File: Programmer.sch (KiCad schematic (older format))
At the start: 59 parts, among them CON1 USB_OTG, M1 ESP-12E, P1 Test, P3 CONN_12, Q1 MMBT3904, Q2 MMBT3906, Q3 MMBT3904, SW1 Upload, SW2 RESET, U1 AP2112K-3.3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

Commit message: Desing Review V00B
Corrections made from doing a Design Review.
Now at revision 00B
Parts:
- removed P1: Test, Measurement_Points:Measurement_Point_Square-TH_Big, symbol CONN_01X01
- added C17: 100 µF, Capacitors_SMD:C_1206_HandSoldering, symbol C
- added C20: 0.1 µF, Capacitors_SMD:C_1206_HandSoldering, symbol C
- added P1: CONN_01X12, symbol CONN_01X12
- added R10, R17, R18, R7: 1K, symbol R
- added R5: 10, symbol R
- C15: value 0.1. µF -> 0.1 µF
- gave numbers to parts that had none: 11
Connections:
- net labels added: IO2, IO3, MISO, MOSI, Pulse, SCK
- wire segments 312 -> 345
- no-connect marks 10 -> 6
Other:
- moved on the sheet: C11, C14, D1, L1, Q4, Q5, R6, R8, R9

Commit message: Re-layout Update V00B
Multiple changes to the schematic and PCB component placement, complete
re-route of PCB.
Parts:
- removed C15, C8, C9: 0.1 µF, Capacitors_SMD:C_1206_HandSoldering, symbol C
- removed U3, U4, U5, U6: 74LVC2T45, Housings_SSOP:MSOP-8_3x3mm_Pitch0.65mm, symbol 74LVC2T45
- removed U7: 74HC595, SMD_Packages:SO-16-N, symbol 74HC595
- added U3: FXMA108, Uprogrammer FPs:DQFN20, symbol FXMA108
- C1, C10, C11, C12, C13, C14, C16, C17, C18, C19, C2, C20, C3, C4, C5, C6, C7: footprint Capacitors_SMD:C_1206_HandSoldering -> Capacitors_SMD:C_1206
- L1: footprint Choke_SMD:Choke_SMD_1206_Handsoldering -> Choke_SMD:Choke_SMD_1206_Standard
- P1: footprint (none) -> Socket_Strips:Socket_Strip_Straight_1x12
- Q4, Q5: footprint (none) -> Housings_SOT-23_SOT-143_TSOT-6:SOT-23
- R1, R11, R12, R13, R14, R15, R16, R19, R2, R20, R3, R4, R6, R8, R9: footprint Resistors_SMD:R_1206_HandSoldering -> Resistors_SMD:R_1206
- R10, R17, R18, R5, R7: footprint (none) -> Resistors_SMD:R_1206
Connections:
- net labels added: Vpf
- net labels removed: D0, D1, D2, D3
- wire segments 345 -> 227
- no-connect marks 6 -> 4
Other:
- note removed: "Assign Pin 11 to VPP \nonce Implimented"
- moved on the sheet: C6

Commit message: V00b PCB fixes
Fixes needed to repair mistakes in PCB design.
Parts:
- removed Q1, Q6, Q7: MMBT3904, Housings_SOT-23_SOT-143_TSOT-6:SOT-23, symbol MMBT3904
- added Q1: BSS138L, Housings_SOT-23_SOT-143_TSOT-6:SOT-23, symbol Q_NMOS_GSD
- R8: value 58.2K -> 100K
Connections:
- wire segments 227 -> 219
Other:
- moved on the sheet: C12, C13, C3, R20
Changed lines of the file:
@@
 P 4875 6525
 F 0 "R8" H 4975 6575 50  0000 C CNN
-F 1 "58.2K" H 5025 6475 50  0000 C CNN
+F 1 "100K" H 5025 6475 50  0000 C CNN
 F 2 "Resistors_SMD:R_1206" V 4805 6525 30  0001 C CNN
 F 3 "" H 4875 6525 30  0000 C CNN
@@
 	2550 2200 2450 2200
 Wire Wire Line
-	2450 2200 2450 2050
+	2450 2050 2450 2200
 Connection ~ 2450 2050
 Connection ~ 2300 2050
@@
 Wire Wire Line
 	6400 700  7550 700
-$Comp
-L MMBT3904 Q1
-U 1 1 55D843D6
-P 8700 4600
-F 0 "Q1" H 8900 4675 50  0000 L CNN
-F 1 "MMBT3904" H 8900 4600 50  0000 L CNN
-F 2 "Housings_SOT-23_SOT-143_TSOT-6:SOT-23" H 8900 4525 50  0001 L CIN
-F 3 "" H 8700 4600 50  0000 L CNN
-	1    8700 4600
-	1    0    0    -1
-$EndComp
 $Comp
 L MMBT3904 Q3
@@
 	4375 3000 4375 2600
 Connection ~ 4375 2600
-Wire Wire Line
-	5600 4300 5950 4300
 Connection ~ 5950 1400
 Wire Wire Line
@@
 ~RST
 $Comp
-L MMBT3904 Q6
-U 1 1 563E70E3
-P 5150 4200
-F 0 "Q6" H 5350 4275 50  0000 L CNN
-F 1 "MMBT3904" H 5350 4200 50  0000 L CNN
-F 2 "Housings_SOT-23_SOT-143_TSOT-6:SOT-23" H 5350 4125 50  0001 L CIN
-F 3 "" H 5150 4200 50  0000 L CNN
-	1    5150 4200
-	1    0    0    -1
-$EndComp
-$Comp
 L R R19
 U 1 1 563E70E9
@@
 $EndComp
 Wire Wire Line
-	4850 4200 4950 4200
-$Comp
-L MMBT3904 Q7
-U 1 1 563E7206
-P 5500 4600
-F 0 "Q7" H 5750 4725 50  0000 L CNN
-F 1 "MMBT3904" H 5725 4650 50  0000 L CNN
-F 2 "Housings_SOT-23_SOT-143_TSOT-6:SOT-23" H 5700 4525 50  0001 L CIN
-F 3 "" H 5500 4600 50  0000 L CNN
-	1    5500 4600
-	1    0    0    -1
-$EndComp
+	4850 4200 5125 4200
 $Comp
 L R R20
 U 1 1 563E720C
-P 5050 4600
-F 0 "R20" V 4900 4575 50  0000 C CNN
-F 1 "10K" V 4975 4575 50  0000 C CNN
-F 2 "Resistors_SMD:R_1206" V 4980 4600 30  0001 C CNN
-F 3 "" H 5050 4600 30  0000 C CNN
-	1    5050 4600
-	0    1    1    0
-$EndComp
-Wire Wire Line
-	5200 4600 5300 4600
-$Comp
-L GND #PWR022
-U 1 1 563E73B6
-P 5600 4850
-F 0 "#PWR022" H 5600 4850 30  0001 C CNN
-F 1 "GND" H 5600 4780 30  0001 C CNN
-F 2 "" H 5600 4850 60  0000 C CNN
-F 3 "" H 5600 4850 60  0000 C CNN
-	1    5600 4850
-	1    0    0    -1
-$EndComp
-$Comp
-L GND #PWR023
-U 1 1 563E7504
-P 5250 4450
-F 0 "#PWR023" H 5250 4450 30  0001 C CNN
-F 1 "GND" H 5250 4380 30  0001 C CNN
-F 2 "" H 5250 4450 60  0000 C CNN
-F 3 "" H 5250 4450 60  0000 C CNN
-	1    5250 4450
-	1    0    0    -1
-$EndComp
-Wire Wire Line
-	5250 4400 5250 4450
-Wire Wire Line
-	5600 4800 5600 4850
-Wire Wire Line
-	4400 4300 4800 4300
+P 5350 4300
+F 0 "R20" V 5200 4275 50  0000 C CNN
+F 1 "10K" V 5275 4275 50  0000 C CNN
+F 2 "Resistors_SMD:R_1206" V 5280 4300 30  0001 C CNN
+F 3 "" H 5350 4300 30  0000 C CNN
+	1    5350 4300
+	0    1    1    0
+$EndComp
 Wire Wire Line
 	4400 4200 4550 4200
-Wire Wire Line
-	5250 3950 5425 3950
-Text Label 5275 3950 0    60   ~ 0
+Text Label 4975 4200 0    60   ~ 0
 ~RST
-$Comp
-L +BATT #PWR024
-U 1 1 563ED62D
-P 4500 3850
-F 0 "#PWR024" H 4500 3800 20  0001 C CNN
-F 1 "+BATT" H 4500 3950 30  0000 C CNN
-F 2 "" H 4500 3850 60  0000 C CNN
-F 3 "" H 4500 3850 60  0000 C CNN
-	1    4500 3850
-	1    0    0    -1
-$EndComp
 Wire Wire Line
 	4500 4000 4400 4000
@@
 Connection ~ 2775 6275
 Connection ~ 3175 6600
-Wire Wire Line
-	5600 4300 5600 4400
-Wire Wire Line
-	4800 4300 4800 4600
-Wire Wire Line
-	4800 4600 4900 4600
-Wire Wire Line
-	5250 3950 5250 4000
 $Comp
 L C C3
 U 1 1 563DA479
-P 3375 4000
-F 0 "C3" V 3225 3850 40  0000 L CNN
-F 1 "0.1 µF" V 3275 3850 40  0000 L CNN
-F 2 "Capacitors_SMD:C_1206" H 3413 3850 30  0001 C CNN
-F 3 "~" H 3375 4000 60  0000 C CNN
-	1    3375 4000
-	0    1    1    0
-$EndComp
-Wire Wire Line
-	3225 4000 2975 4000
+P 3250 4000
+F 0 "C3" V 3100 3850 40  0000 L CNN
+F 1 "0.1 µF" V 3150 3850 40  0000 L CNN
+F 2 "Capacitors_SMD:C_1206" H 3288 3850 30  0001 C CNN
+F 3 "~" H 3250 4000 60  0000 C CNN
+	1    3250 4000
+	0    1    1    0
+$EndComp
+Wire Wire Line
+	3100 4000 2975 4000
 Connection ~ 2975 4600
 Wire Wire Line
-	3525 4000 3600 4000
+	3400 4000 3600 4000
 $Comp
 L C C12
 U 1 1 563E29A5
-P 3375 3475
-F 0 "C12" V 3225 3325 40  0000 L CNN
-F 1 "10 µF" V 3275 3325 40  0000 L CNN
-F 2 "Capacitors_SMD:C_1206" H 3413 3325 30  0001 C CNN
-F 3 "~" H 3375 3475 60  0000 C CNN
-	1    3375 3475
+P 3250 3475
+F 0 "C12" V 3100 3325 40  0000 L CNN
+F 1 "10 µF" V 3150 3325 40  0000 L CNN
+F 2 "Capacitors_SMD:C_1206" H 3288 3325 30  0001 C CNN
+F 3 "~" H 3250 3475 60  0000 C CNN
+	1    3250 3475
 	0    1    1    0
 $EndComp
@@
 L C C13
 U 1 1 563E2B59
-P 3375 3725
-F 0 "C13" V 3225 3575 40  0000 L CNN
-F 1 "0.1 µF" V 3275 3575 40  0000 L CNN
-F 2 "Capacitors_SMD:C_1206" H 3413 3575 30  0001 C CNN
-F 3 "~" H 3375 3725 60  0000 C CNN
-	1    3375 3725
-	0    1    1    0
-$EndComp
-Wire Wire Line
-	3225 3475 2975 3475
+P 3250 3725
+F 0 "C13" V 3100 3575 40  0000 L CNN
+F 1 "0.1 µF" V 3150 3575 40  0000 L CNN
+F 2 "Capacitors_SMD:C_1206" H 3288 3575 30  0001 C CNN
+F 3 "~" H 3250 3725 60  0000 C CNN
+	1    3250 3725
+	0    1    1    0
+$EndComp
+Wire Wire Line
+	3100 3475 2975 3475
 Connection ~ 2975 4000
 Wire Wire Line
-	3225 3725 2975 3725
+	3100 3725 2975 3725
 Connection ~ 2975 3725
 Wire Wire Line
-	3525 3725 4025 3725
+	3400 3725 4025 3725
 Wire Wire Line
 	4025 3725 4025 3900
@@
 Connection ~ 4500 3900
 Wire Wire Line
-	3525 3475 3575 3475
-Wire Wire Line
-	3575 3475 3575 3725
-Connection ~ 3575 3725
+	3400 3475 3525 3475
+Wire Wire Line
+	3525 3475 3525 4000
+Connection ~ 3525 3725
 NoConn ~ 3600 4100
 Wire Wire Line
@@
 	6800 1900 6800 3400
 Wire Wire Line
-	6900 2300 5900 2300
+	5900 2300 6900 2300
 Wire Wire Line
 	6700 3300 6700 2300
@@
 Wire Wire Line
 	6100 4600 8100 4600
+$Comp
+L Q_NMOS_GSD Q1
+U 1 1 5688527A
+P 8700 4600
+F 0 "Q1" H 8550 4825 50  0000 R CNN
+F 1 "BSS138L" H 8775 4750 50  0000 R CNN
+F 2 "Housings_SOT-23_SOT-143_TSOT-6:SOT-23" H 8900 4700 29  0001 C CNN
+F 3 "" H 8700 4600 60  0000 C CNN
+	1    8700 4600
+	1    0    0    -1
+$EndComp
+Wire Wire Line
+	5950 4300 5500 4300
+Wire Wire Line
+	5200 4300 4400 4300
+Connection ~ 3525 4000
+$Comp
+L 3V3 #PWR?
+U 1 1 56893110
+P 4500 3850
+F 0 "#PWR?" H 4500 3950 40  0001 C CNN
+F 1 "3V3" H 4500 3975 40  0000 C CNN
+F 2 "" H 4500 3850 60  0000 C CNN
+F 3 "" H 4500 3850 60  0000 C CNN
+	1    4500 3850
+	1    0    0    -1
+$EndComp
 $EndSCHEMATC

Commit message: Hardware V00C
Design Update to start testing a lithium polimer cell as my power
source. Added a charge management IC that charges as well as supplies
system voltage.
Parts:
- removed BT1: BATTERY, Connect:PINHEAD1-2, symbol BATTERY
- added BT1: LiPo, symbol Single_cell
- added C15, C8: 1 µF, Capacitors_SMD:C_1206, symbol C
- added C9: 0.1 uF, Capacitors_SMD:C_1206, symbol C
- added D2: Red, symbol Led_Small
- added D3: Green, symbol Led_Small
- added D4: SD103, Diodes_SMD:SOD-323, symbol D_Schottky_Small
- added Q6: MMBT3906, Housings_SOT-23_SOT-143_TSOT-6:SOT-23, symbol MMBT3906
- added R21: 150K, symbol R
- added R22, R26: 100K, symbol R
- added R23: 10K, symbol R
- added R24, R25: 200, symbol R
- added R27: 22K, symbol R
- added U4: AAT3672-4.2-1, symbol AAT3672-4.2-1
- R4: value 10K -> 22K
- R5: value 10 -> 1K
- U8: symbol CH340G -> CH340G-RESCUE-Programmer
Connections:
- net labels added: +5V, MTDO
- wire segments 219 -> 265
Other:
- moved on the sheet: C1, C10, C11, C12, C13, C14, C16, C17, C18, C19, C2, C20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

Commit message: Hardware V00D
Revisions found during design review
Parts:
- removed R19, R20: 10K, Resistors_SMD:R_1206, symbol R
- added L2: 2.2 µH, Choke_SMD:Choke_SMD_1206_Standard, symbol INDUCTOR
- added Q? (x2): MMBT3904, Housings_SOT-23_SOT-143_TSOT-6:SOT-23, symbol MMBT3904
- added R? (x2): 10K, Resistors_SMD:R_1206, symbol R
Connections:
- net GND: now also L2.2; no longer C11.2, C14.2, C17.2, C20.2, Q5.2 (S), R9.2
- net at U8.13 (~DTR): now also Q?.2 (E), R?.2
- net at U8.14 (~RTS): now also Q?.2 (E), R?.2
- new net: Q?.1 (B), R?.1 (x2)
- new net GNDpp: C11.2, C14.2, C17.2, C20.2, L2.1, Q5.2 (S), R9.2
- no-connect marks 4 -> 2
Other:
- note added: "If U2 doesn't seem to work \nor is unreliable R27 may \nbe too big"
- note added: "The level shifter needs tested."
- moved on the sheet: C11, C14, C17, C20, D1, L1, Q4, Q5, R5, R6, R8, R9

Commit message: New Layout V00E
Updated layout with newest schematic design.
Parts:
- removed R1: 10K, Resistors_SMD:R_1206, symbol R
- removed SW1: Upload, Buttons_Switches_SMD:SW_SPST_PTS645, symbol SW_PUSH
- added C21: 10 µF, Capacitors_SMD:C_1206, symbol C
- BT1: footprint (none) -> Connect:PINHEAD1-2
- D2, D3: footprint (none) -> LEDs:LED_1206
- Q1, Q2, Q3, Q4, Q5, Q6: footprint Housings_SOT-23_SOT-143_TSOT-6:SOT-23 -> TO_SOT_Packages_SMD:SOT-23
- Q7, Q8: renamed from Q?; footprint Housings_SOT-23_SOT-143_TSOT-6:SOT-23 -> TO_SOT_Packages_SMD:SOT-23
- R21, R22, R23, R24, R25, R26, R27: footprint (none) -> Resistors_SMD:R_1206
- U1: footprint Housings_SOT-23_SOT-143_TSOT-6:SOT-23-5 -> TO_SOT_Packages_SMD:SOT-23-5
- U10: footprint Housings_SOT-23_SOT-143_TSOT-6:SC-70-6_Handsoldering -> TO_SOT_Packages_SMD:SC-70-6
- U4: footprint (none) -> UprogrammerFPs:DFN-14-1EP_3x3mm_Pitch0.4mm
- gave numbers to parts that had none: 2
- renumbered SW2 to SW1
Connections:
- net +5V: no longer U4.8 (ENBAT)
- net GND: now also C21.2
- net ~RST: now also Q7.3 (C)
- net at M1.18 (GPIO0), U10.6: now also Q8.3 (C)
- net at BT1.1, U4.12 (BAT): now also U4.8 (ENBAT), C21.1
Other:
- moved on the sheet: BT1, R23

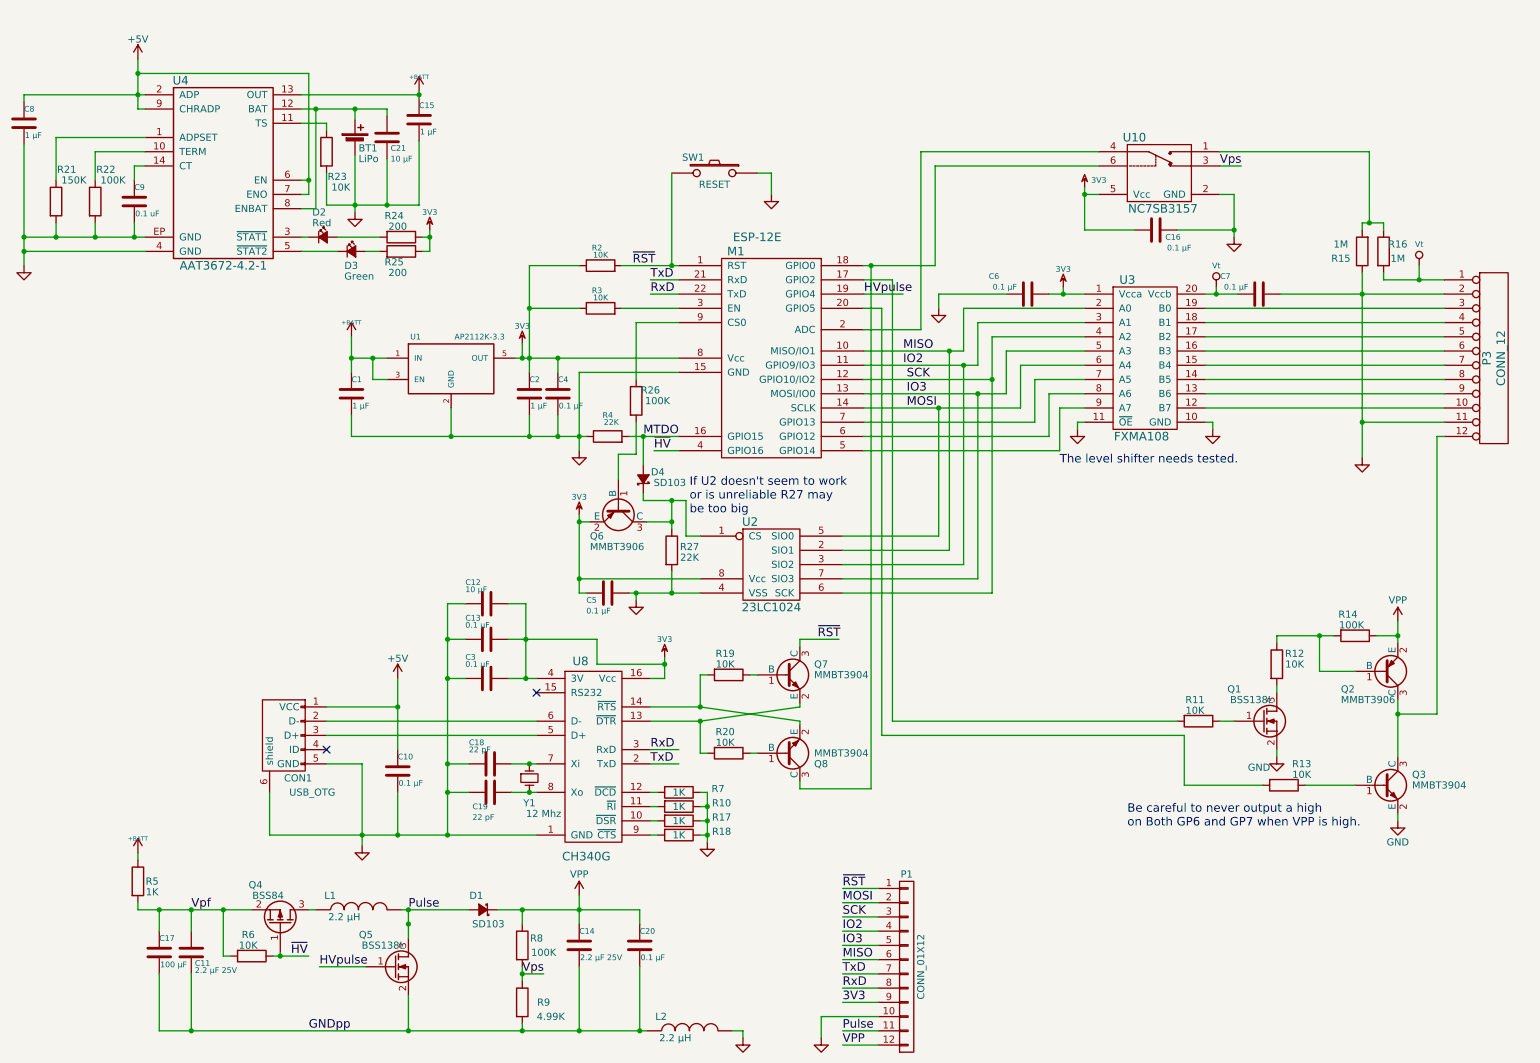
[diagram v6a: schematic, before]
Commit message: Hardware V00G
Changed value of R5 from 100 to 47 Ohms. This improves the voltage boost
functionality.
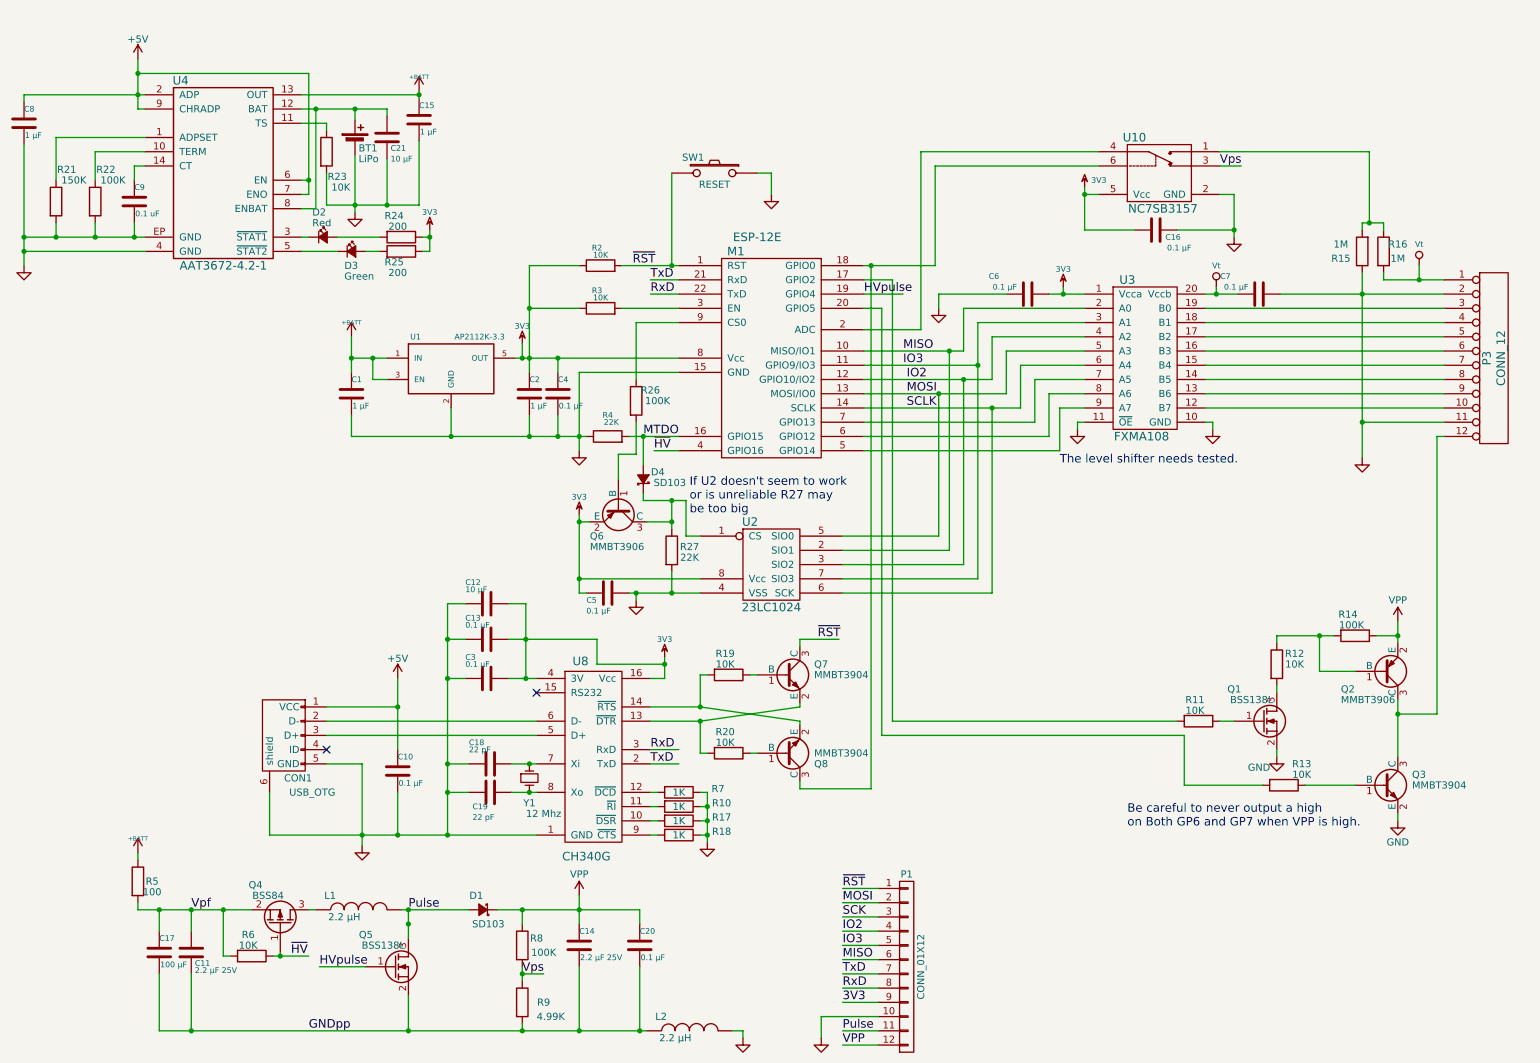
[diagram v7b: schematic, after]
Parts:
- R5: value 1K -> 100
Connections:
- net IO2: now also M1.12 (GPIO10/IO2), U3.4 (A2); no longer M1.11 (GPIO9/IO3), U3.3 (A1)
- net IO3: now also M1.11 (GPIO9/IO3), U3.3 (A1); no longer M1.13 (MOSI/IO0), U3.5 (A3)
- net MOSI: now also M1.13 (MOSI/IO0), U3.5 (A3); no longer M1.14 (SCLK), U3.6 (A4)
- net SCK: no longer M1.12 (GPIO10/IO2), U2.6 (SCK), U3.4 (A2)
- new net SCLK: M1.14 (SCLK), U2.6 (SCK), U3.6 (A4)
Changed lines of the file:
@@
 SCK
 Text Label 6800 3025 0    60   ~ 0
-SCK
+IO2
 Text Label 6800 3225 0    60   ~ 0
-MOSI
+SCLK
 Text Label 6775 2825 0    60   ~ 0
 MISO
 Text Label 6775 2925 0    60   ~ 0
-IO2
+IO3
 Text Label 6800 3125 0    60   ~ 0
-IO3
+MOSI
 Text Label 6350 6700 0    60   ~ 0
 MOSI
@@
 P 1400 6550
 F 0 "R5" H 1500 6550 50  0000 C CNN
-F 1 "1K" H 1500 6475 50  0000 C CNN
+F 1 "100" H 1500 6475 50  0000 C CNN
 F 2 "Resistors_SMD:R_1206" V 1330 6550 30  0001 C CNN
 F 3 "" H 1400 6550 30  0000 C CNN
@@
 	6500 2825 7200 2825
 Wire Wire Line
-	7300 2925 7300 2625
-Wire Wire Line
-	7400 2725 7400 4525
+	7300 2625 7300 4425
 Wire Wire Line
 	6500 3125 7500 3125
-Wire Wire Line
-	7300 4425 7300 3125
-Connection ~ 7300 3125
-Connection ~ 7400 3025
-Wire Wire Line
-	7200 4325 7200 2925
-Connection ~ 7200 2925
-Wire Wire Line
-	7100 4225 7100 2825
-Connection ~ 7100 2825
-Wire Wire Line
-	7025 4125 7025 3225
-Connection ~ 7025 3225
 Text Label 1775 6750 0    60   ~ 0
 Vpf
@@
 Wire Wire Line
 	5850 1575 5750 1575
+Wire Wire Line
+	7400 3025 7400 2725
+Wire Wire Line
+	7025 4125 7025 3125
+Connection ~ 7025 3125
+Wire Wire Line
+	7100 4225 7100 2825
+Connection ~ 7100 2825
+Wire Wire Line
+	7200 4325 7200 3025
+Connection ~ 7200 3025
+Connection ~ 7300 2925
+Wire Wire Line
+	7400 4525 7400 3225
+Connection ~ 7400 3225
 $EndSCHEMATC
